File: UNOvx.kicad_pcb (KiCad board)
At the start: 2 copper layers, 72 x 53.5 mm, 38 parts, among them IC1 BTS462T, J1 Barrel_Jack_Switch, J2 Ext. Power, J3 Conn_01x02_Male, J4 Conn_02x03_Odd_Even, P1 Analog, P2 Power, P3 Digital, P4 Digital, P5 CONN_01X01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

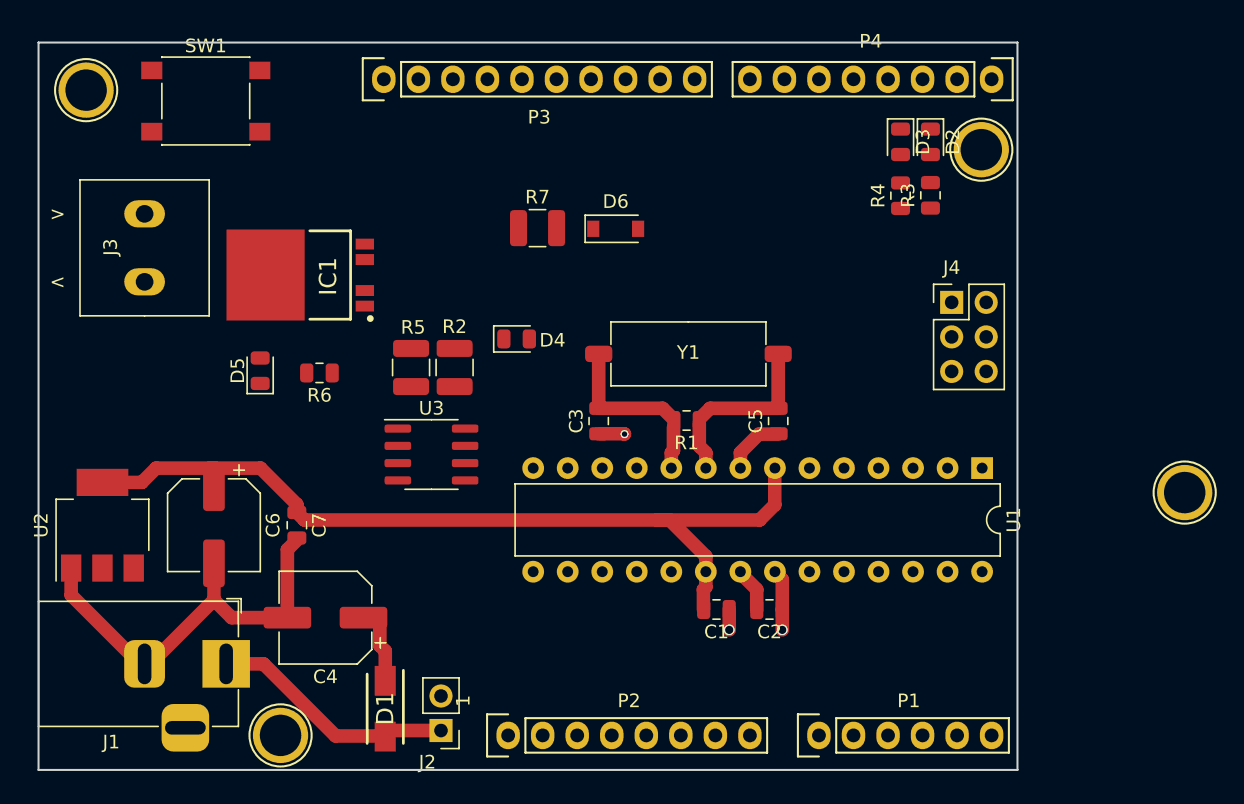
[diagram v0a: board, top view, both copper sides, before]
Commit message: Route the switch
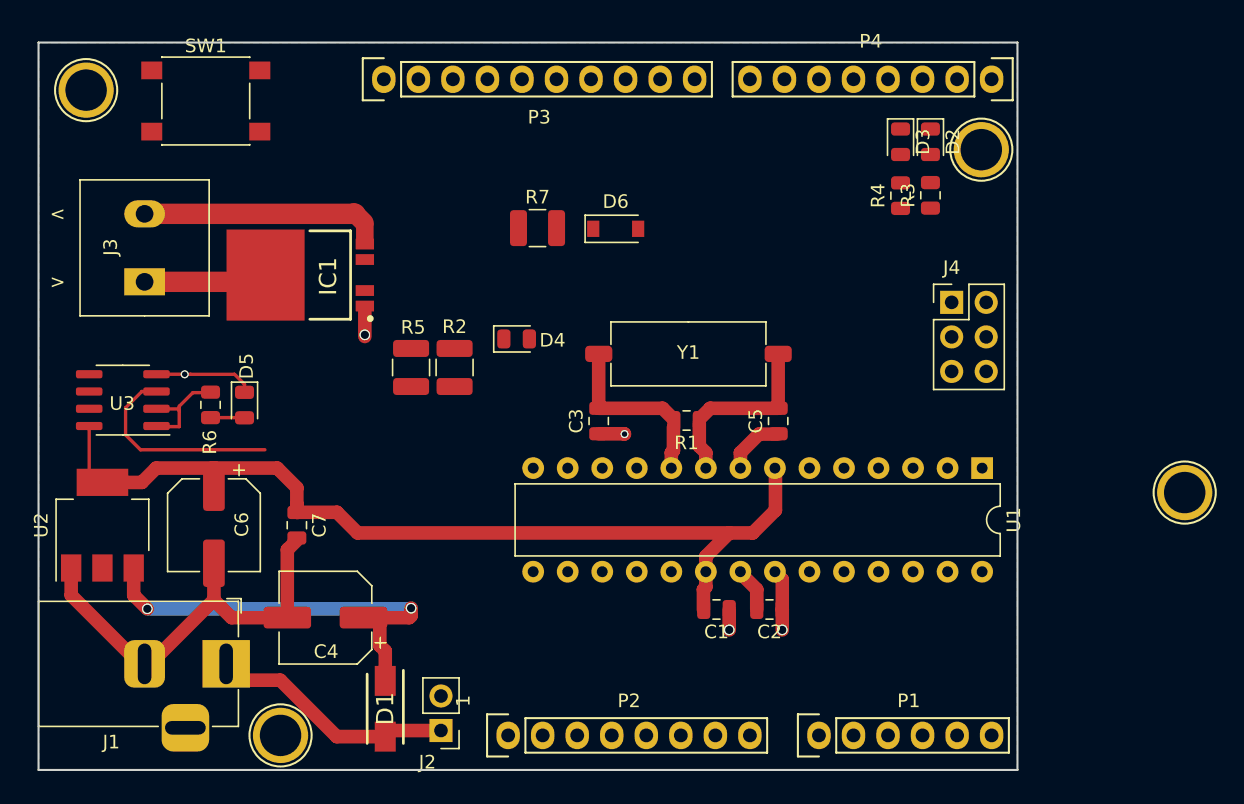
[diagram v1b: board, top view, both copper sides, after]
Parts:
- IC1: footprint TO-252-5PIN -> kicad-lib:TO-252-5PIN
- moved U3 23.0 mm to (113.9, 99.2), turned to 180 degrees
- moved R6 8.35 mm to (120.3, 99.5), turned to 270 degrees
- moved D5 2.77 mm to (122.8, 99.5), turned to 270 degrees
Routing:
- net Net-(C4-Pad1): track 4.62 -> 30.5 mm, vias 0 -> 2
- net Net-(IC1-Pad5): track 0.00 -> 17.6 mm
- net PB5(SCK): track 0.00 -> 15.5 mm
- net GND: track 42.7 -> 52.2 mm, vias 3 -> 5
- net Net-(IC1-Pad3): track 0.00 -> 7.45 mm
- net Net-(R6-Pad1): track 0.00 -> 6.26 mm
- net +5V: track 64.1 -> 67.0 mm
- net Net-(D5-Pad2): track 0.00 -> 2.49 mm
- added copper zone on B.Cu, net GND

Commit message: Move power LED
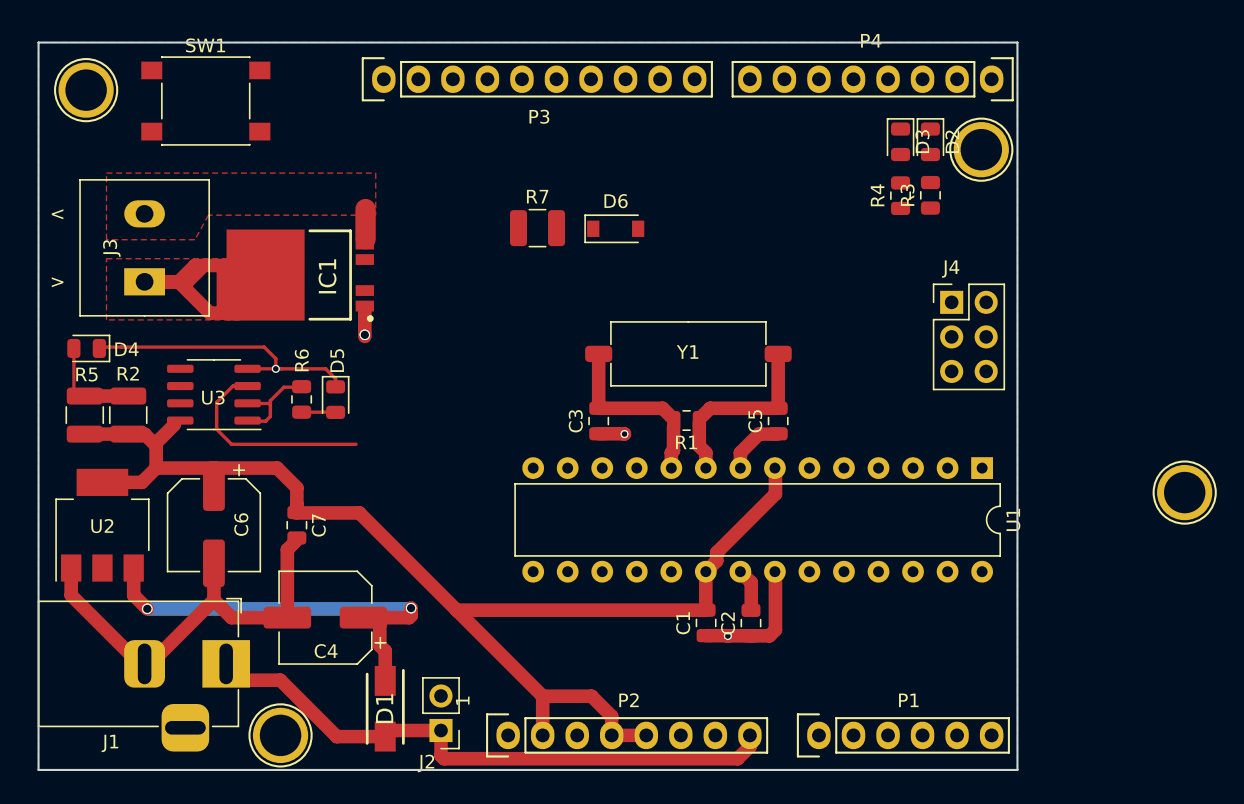
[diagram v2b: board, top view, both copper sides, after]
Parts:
- moved D4 31.6 mm to (111.2, 95.4), turned to 180 degrees
- moved R5 24.3 mm to (111.1, 100.3)
- moved R2 24.3 mm to (114.3, 100.3)
- moved D5 6.71 mm to (129.5, 99.1)
- moved R6 6.71 mm to (127.0, 99.1)
- moved U3 6.71 mm to (120.6, 98.8)
- moved C2 1.69 mm to (160.1, 115.6), turned to 90 degrees
- moved C1 1.25 mm to (156.8, 115.6), turned to 90 degrees
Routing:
- net +5V: track 67.0 -> 92.9 mm
- net Vin: track 17.8 -> 43.8 mm
- net GND: track 52.2 -> 69.9 mm, vias 5 -> 4
- net Net-(IC1-Pad5): track 17.6 -> 2.22 mm
- net Net-(IC1-Pad3): track 7.45 -> 20.2 mm
- net Net-(D4-Pad2): track 0.00 -> 6.50 mm
- added copper zone on F.Cu, net Net-(IC1-Pad3)
- added copper zone on F.Cu, net Net-(IC1-Pad5)

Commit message: ADC lines
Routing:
- net A5(SCL): track 0.00 -> 12.3 mm
- net A3: track 0.00 -> 12.3 mm
- net A2: track 0.00 -> 12.3 mm
- net A0: track 0.00 -> 12.3 mm
- net A4(SDA): track 0.87 -> 13.2 mm
- net A1: track 0.00 -> 12.3 mm
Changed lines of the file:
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@@
     (thickness 1.6)
     (drawings 11)
-    (tracks 127)
+    (tracks 145)
     (zones 0)
     (modules 38)
@@
   )
   (setup
-    (last_trace_width 1)
+    (last_trace_width 0.25)
     (user_trace_width 1)
     (user_trace_width 1.5)
@@
     (descr "Through hole socket strip")
     (tags "socket strip")
-    (fp_text reference P1 (at 6.604 -2.54) (layer F.SilkS)
+    (fp_text reference P1 (at 5.85 -2.56) (layer F.SilkS)
       (effects (font (size 1 1) (thickness 0.15)))
     )
@@
   (gr_line (start 107.698 126.365) (end 179.698 126.365) (angle 90) (layer Edge.Cuts) (width 0.15))
   (gr_line (start 179.698 72.865) (end 107.698 72.865) (angle 90) (layer Edge.Cuts) (width 0.15))
+  (segment (start 165.078 123.775) (end 165.078 122.509) (width 0.25) (layer F.Cu) (net 26))
+  (segment (start 165.078 122.509) (end 164.398 121.829) (width 0.25) (layer F.Cu) (net 26))
+  (segment (start 164.398 121.829) (end 164.398 111.765) (width 0.25) (layer F.Cu) (net 26))
+  (segment (start 167.628 123.775) (end 167.628 122.509) (width 0.25) (layer F.Cu) (net 27))
+  (segment (start 167.628 122.509) (end 166.948 121.829) (width 0.25) (layer F.Cu) (net 27))
+  (segment (start 166.948 121.829) (end 166.948 111.765) (width 0.25) (layer F.Cu) (net 27))
+  (segment (start 170.178 123.775) (end 170.178 122.509) (width 0.25) (layer F.Cu) (net 28))
+  (segment (start 170.178 122.509) (end 169.498 121.829) (width 0.25) (layer F.Cu) (net 28))
+  (segment (start 169.498 121.829) (end 169.498 111.765) (width 0.25) (layer F.Cu) (net 28))
+  (segment (start 175.278 123.775) (end 175.278 122.509) (width 0.25) (layer F.Cu) (net 30))
+  (segment (start 175.278 122.509) (end 174.598 121.829) (width 0.25) (layer F.Cu) (net 30))
+  (segment (start 174.598 121.829) (end 174.598 111.765) (width 0.25) (layer F.Cu) (net 30))
+  (segment (start 172.728 123.775) (end 172.728 122.509) (width 0.25) (layer F.Cu) (net 29))
+  (segment (start 172.728 122.509) (end 172.048 121.829) (width 0.25) (layer F.Cu) (net 29))
+  (segment (start 172.048 121.829) (end 172.048 111.765) (width 0.25) (layer F.Cu) (net 29))
   (segment (start 115.298 105.215) (end 116.348 104.165) (width 1) (layer F.Cu) (net 1))
   (segment (start 112.398 105.215) (end 115.298 105.215) (width 1) (layer F.Cu) (net 1))
@@
   (segment (start 121.898 102.415) (end 131.048 102.415) (width 0.25) (layer F.Cu) (net 24))
   (segment (start 174.680999 123.247999) (end 175.298 123.865) (width 0.25) (layer B.Cu) (net 30))
+  (segment (start 177.148 121.829) (end 177.148 111.765) (width 0.25) (layer F.Cu) (net 31))
+  (segment (start 177.828 123.775) (end 177.828 122.509) (width 0.25) (layer F.Cu) (net 31))
+  (segment (start 177.828 122.509) (end 177.148 121.829) (width 0.25) (layer F.Cu) (net 31))
   (segment (start 124.598 99.415) (end 123.548 99.415) (width 0.25) (layer F.Cu) (net 41))
   (segment (start 124.748 99.565) (end 124.748 99.215) (width 0.25) (layer F.Cu) (net 41))
